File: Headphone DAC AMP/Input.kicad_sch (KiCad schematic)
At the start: 2 parts, among them J1 USB_C_Receptacle, U2 XU316-1024-QF60B-C24

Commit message: Updating Changes
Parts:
- added C10, C11, C12, C13, C14, C15, C16, C17, C9: 100nf, symbol Device:C
- added U8: W25Q16JVSNIQ, SOIC_150MIL_WIN, symbol W25Q16JVSNIQ:W25Q16JVSNIQ
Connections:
- net QSPI_D1: now reaches U2.1 (X0D05)
- net QSPI_D1: now also U8.2 (DO(IO1))
- net QSPI_D3: now reaches U2.2 (X0D07)
- net QSPI_D3: now also U8.7 (/HOLD_/RESET)
- net QSPI_CSN: now reaches U2.3 (X0D01)
- net QSPI_CSN: now also U8.1 (/CS)
- net QSPI_CLK: now reaches U2.5 (X0D10)
- net QSPI_CLK: now also U8.6 (CLK)
- net QSPI_D0: now reaches U2.59 (X0D04)
- net QSPI_D0: now also U8.5 (DI(IO0))
- net QSPI_D2: now reaches U2.60 (X0D06)
- net QSPI_D2: now also U8.3 (/WP(IO2))
- new net +3.3V: C10.1, C11.1, C12.1, C13.1, C14.1, C15.1, C16.1, C17.1, C9.1, U8.8 (VCC)
- new net GND: C10.2, C11.2, C12.2, C13.2, C14.2, C15.2, C16.2, C17.2, C9.2, U8.4 (GND)
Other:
- moved on the sheet: U2

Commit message: Power Delivery
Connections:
- net RX2-: now reaches J1.A10 (RX2-)
- net RX2+: now reaches J1.A11 (RX2+)
- net TX1+: now reaches J1.A2 (TX1+)
- net TX1-: now reaches J1.A3 (TX1-)
- net VBUS_C: now reaches J1.A4 (VBUS), J1.A9 (VBUS), J1.B4 (VBUS), J1.B9 (VBUS)
- net CC1: now reaches J1.A5 (CC1)
- net D+: now reaches J1.A6 (D+)
- net D+: now also J1.B6 (D+), U2.29 (USB_DP)
- net D-: now reaches J1.A7 (D-)
- net D-: now also J1.B7 (D-), U2.28 (USB_DM)
- net SBU1: now reaches J1.A8 (SBU1)
- net RX1-: now reaches J1.B10 (RX1-)
- net RX1+: now reaches J1.B11 (RX1+)
- net TX2+: now reaches J1.B2 (TX2+)
- net TX2-: now reaches J1.B3 (TX2-)
- net CC2: now reaches J1.B5 (CC2)
- net SBU2: now reaches J1.B8 (SBU2)
- net VDD: now reaches U2.12 (VDD)
- net VDD: now also U2.19 (VDD), U2.27 (VDD), U2.34 (VDD), U2.4 (VDD), U2.42 (VDD), U2.49 (VDD), U2.57 (VDD), U2.61 (VDD), U2.62 (VDD), U2.63 (VDD), U2.65 (VSS)
- net 1V8 DBG: now reaches U2.17 (VDDIOB18)
- net 1V8 DBG: now also U2.31 (USB_VDD18), U2.38 (VDDIOR), U2.52 (VDDIOT), U2.8 (VDDIOL)
- net 3V3 DBG: now reaches U2.30 (USB_VDD33)

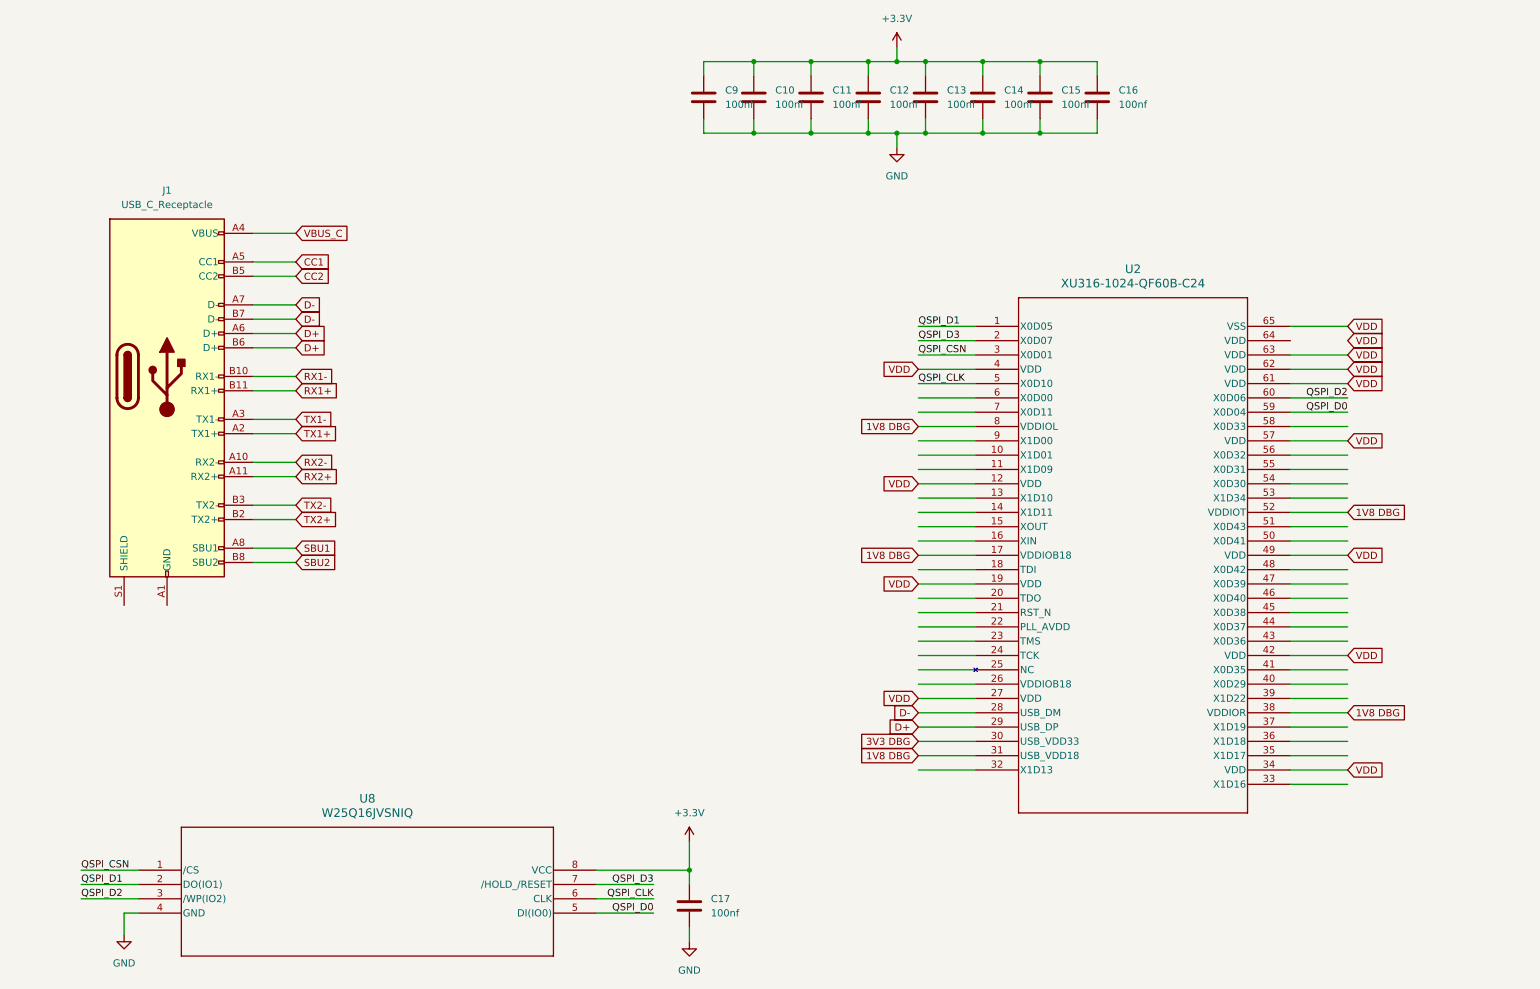
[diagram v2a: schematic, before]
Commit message: Added crystals
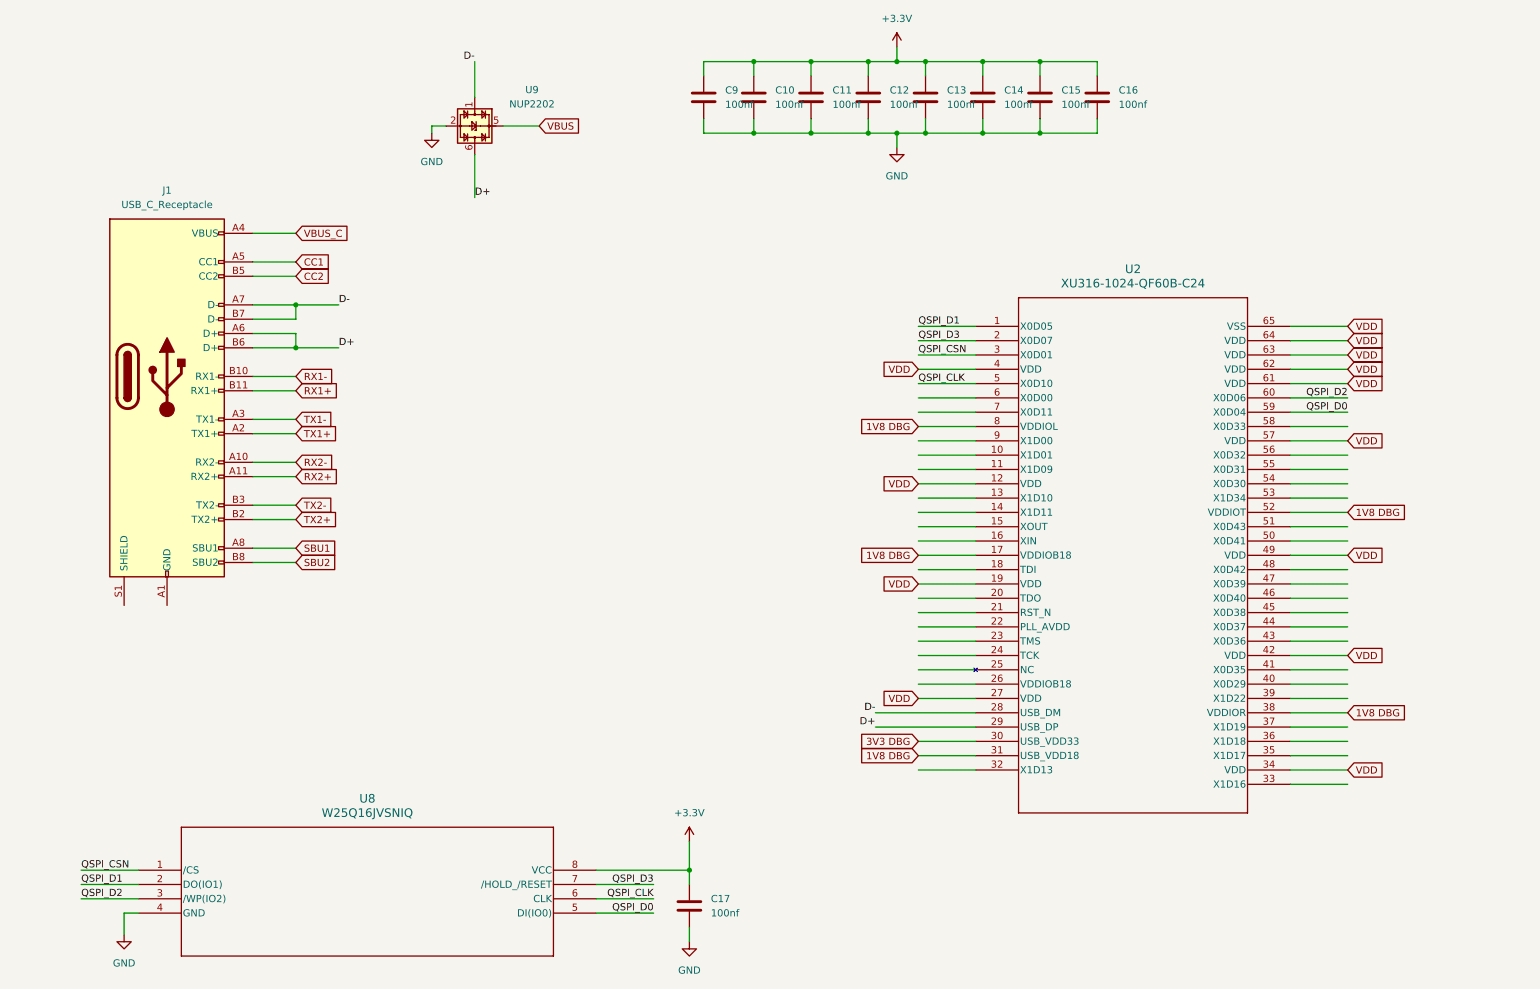
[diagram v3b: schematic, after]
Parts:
- added U9: NUP2202, Package_TO_SOT_SMD:SOT-363_SC-70-6, symbol Power_Protection:NUP2202
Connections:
- net D+: now also U9.6
- net D-: now also U9.1
- net GND: now also U9.2
- net VDD: now also U2.64 (VDD)
- new net VBUS: U9.5

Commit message: Began connecting Root page
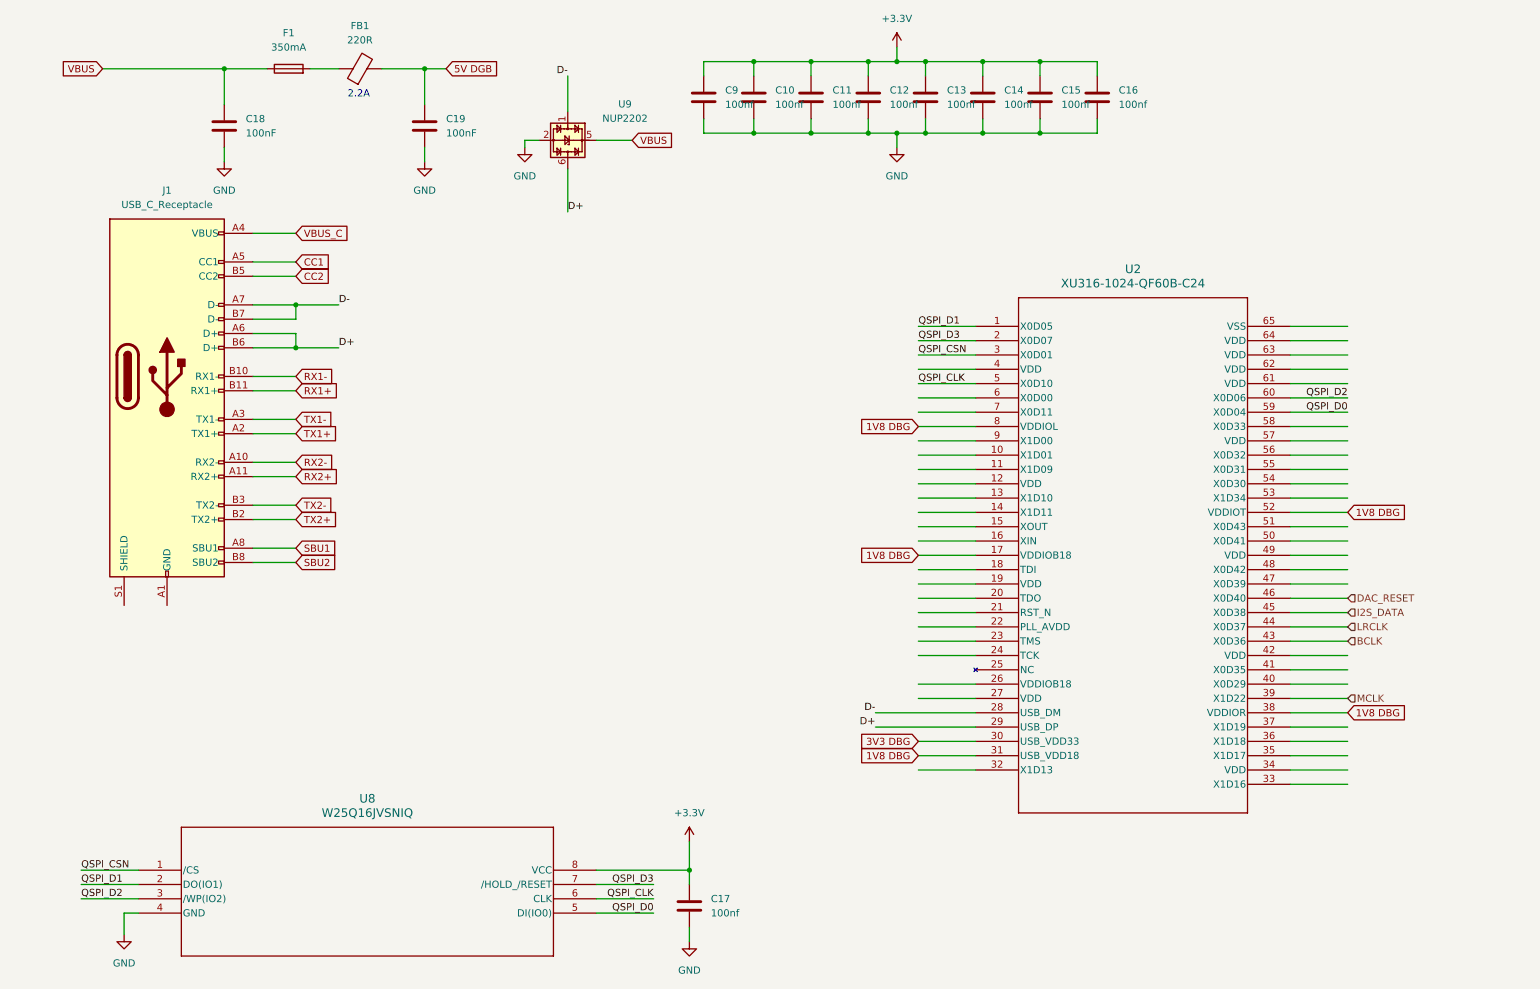
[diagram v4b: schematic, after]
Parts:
- added C18, C19: 100nF, symbol Device:C
- added F1: 350mA, symbol Device:Fuse
- added FB1: 220R, symbol Device:FerriteBead
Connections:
- net GND: now also C18.2, C19.2
- net VBUS: now also C18.1, F1.1
- net MCLK: now reaches U2.39 (X1D22)
- net BCLK: now reaches U2.43 (X0D36)
- net LRCLK: now reaches U2.44 (X0D37)
- net I2S_DATA: now reaches U2.45 (X0D38)
- net DAC_RESET: now reaches U2.46 (X0D40)
- removed net VDD: U2.12 (VDD), U2.19 (VDD), U2.27 (VDD), U2.34 (VDD), U2.4 (VDD), U2.42 (VDD), U2.49 (VDD), U2.57 (VDD), U2.61 (VDD), U2.62 (VDD), U2.63 (VDD), U2.64 (VDD), U2.65 (VSS)
- new net: F1.2, FB1.1
- new net 5V DGB: C19.1, FB1.2
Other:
- note added: "2.2A"
- moved on the sheet: U9

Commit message: Populated pins a bit more
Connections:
- net JTAG_TDI: now reaches U2.18 (TDI)
- net JTAG_TD0: now reaches U2.20 (TDO)
- net JTAG_TMS: now reaches U2.23 (TMS)
- net JTAG_TCK: now reaches U2.24 (TCK)
- net 4D0: now reaches U2.33 (X1D16)
- net 4D1: now reaches U2.34 (VDD)
- net 4D2: now reaches U2.35 (X1D17)
- net 4D3: now reaches U2.36 (X1D18)
- net EN_49: now reaches U2.40 (X0D29)
- net EN45: now reaches U2.54 (X0D30)
- net SCL: now reaches U2.56 (X0D32)
- net SDA/MOSI: now reaches U2.58 (X0D33)
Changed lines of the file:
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@@
+		)
+	)
+	(hierarchical_label "EN_49"
+		(shape input)
+		(at 252.73 130.81 0)
+		(effects
+			(font
+				(size 1.27 1.27)
+			)
+			(justify left)
+		)
+	)
+	(hierarchical_label "SS"
+		(shape input)
+		(at 267.97 71.12 0)
+		(effects
+			(font
+				(size 1.27 1.27)
+			)
+			(justify left)
 		)
 	)
@@
 		)
 	)
+	(hierarchical_label "SDA{slash}MOSI"
+		(shape input)
+		(at 252.73 85.09 0)
+		(effects
+			(font
+				(size 1.27 1.27)
+			)
+			(justify left)
+		)
+	)
+	(hierarchical_label "JTAG_TMS"
+		(shape input)
+		(at 176.53 123.19 180)
+		(effects
+			(font
+				(size 1.27 1.27)
+			)
+			(justify right)
+		)
+	)
+	(hierarchical_label "EN45"
+		(shape input)
+		(at 252.73 95.25 0)
+		(effects
+			(font
+				(size 1.27 1.27)
+			)
+			(justify left)
+		)
+	)
+	(hierarchical_label "JTAG_TDI"
+		(shape input)
+		(at 176.53 110.49 180)
+		(effects
+			(font
+				(size 1.27 1.27)
+			)
+			(justify right)
+		)
+	)
 	(hierarchical_label "LRCLK"
 		(shape input)
@@
 			)
 			(justify left)
+		)
+	)
+	(hierarchical_label "4D2"
+		(shape input)
+		(at 252.73 143.51 0)
+		(effects
+			(font
+				(size 1.27 1.27)
+			)
+			(justify left)
+		)
+	)
+	(hierarchical_label "4D3"
+		(shape input)
+		(at 252.73 140.97 0)
+		(effects
+			(font
+				(size 1.27 1.27)
+			)
+			(justify left)
+		)
+	)
+	(hierarchical_label "4D0"
+		(shape input)
+		(at 252.73 148.59 0)
+		(effects
+			(font
+				(size 1.27 1.27)
+			)
+			(justify left)
+		)
+	)
+	(hierarchical_label "JTAG_TD0"
+		(shape input)
+		(at 176.53 115.57 180)
+		(effects
+			(font
+				(size 1.27 1.27)
+			)
+			(justify right)
+		)
+	)
+	(hierarchical_label "4D1"
+		(shape input)
+		(at 252.73 146.05 0)
+		(effects
+			(font
+				(size 1.27 1.27)
+			)
+			(justify left)
+		)
+	)
+	(hierarchical_label "JTAG_TCK"
+		(shape input)
+		(at 176.53 125.73 180)
+		(effects
+			(font
+				(size 1.27 1.27)
+			)
+			(justify right)
 		)
 	)
@@
 		)
 	)
+	(hierarchical_label "SCL"
+		(shape input)
+		(at 252.73 90.17 0)
+		(effects
+			(font
+				(size 1.27 1.27)
+			)
+			(justify left)
+		)
+	)
 	(hierarchical_label "MCLK"
 		(shape input)
@@
 		(effects
 			(font
+				(size 1.27 1.27)
+			)
+			(justify left)
+		)
+	)
+	(hierarchical_label "MISO"
+		(shape input)
+		(at 267.97 73.66 0)
+		(effects
+			(font
